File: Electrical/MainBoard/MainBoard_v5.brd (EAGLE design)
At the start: 100 x 100 mm, 117 parts, among them IC1 MEGA1284-P, IC2 MCP4922-E/SL, IC3 MCP4921-E/SN, IC4 TL074D, IC5 TL074D, IC6 FT232RL, Q1 BC140-10, Q2 BC160, Q3 BC140-10, Q4 BC160, Q5 BD239, Q6 BC547, Q7 BC557, Q8 16MHz, X1 FH12-45S-0.5SH, X2 22-23-2021, X3 PN61729-S

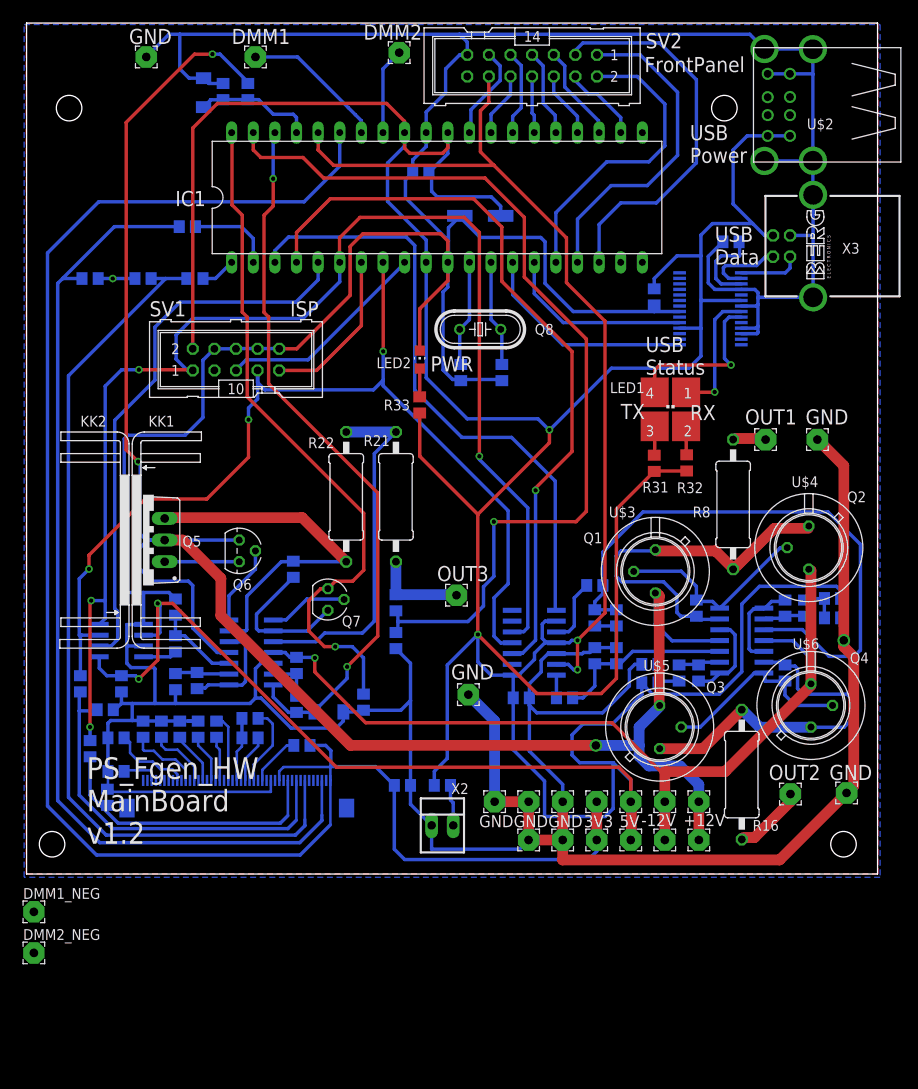
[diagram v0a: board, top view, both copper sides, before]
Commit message: Updated OutputControls and MainBoard in Electrical folder
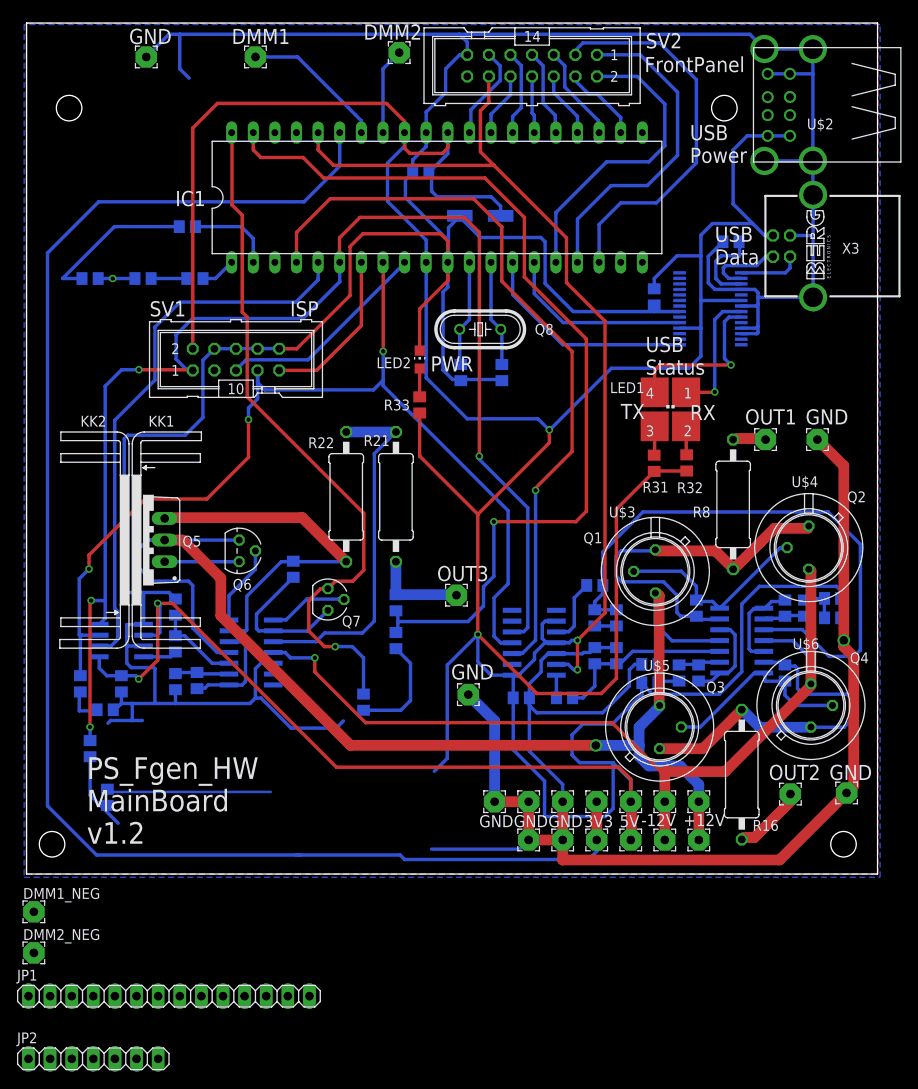
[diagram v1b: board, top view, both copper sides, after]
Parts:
- removed C12, C13, C14, C15, C16, C17, C18, C19, C20, C21, C22: 4u7, rcl:C0805
- removed D3, D4: 5V, diode:SOD80C
- removed R27: 240k, OwnDevices:R0805
- removed R28, R30: 100k, OwnDevices:R0805
- removed R29: 150k, OwnDevices:R0805
- removed R34: 10R, rcl:R0805
- removed X1: FH12-45S-0.5SH, con-hirose:FH12-45S-0.5SH
- removed X2: 22-23-2021, con-molex:22-23-2021
- added JP1: PINHD-1X14, Connector:1X14
- added JP2: PINHD-1X7, Connector:1X07
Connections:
- net LCD_A0 renamed LCD_DC
- removed net !DDS_LDAC: IC1.3, IC2.8
- removed net +12V_VOLT: D4.C, IC1.37, R29.1, R30.2
- removed net -12V_VOLT: D3.C, IC1.38, IC5.14, R28.1
- removed net BL_A: R34.2, X2.2
- removed net CAP1+: C15.1, X1.21
- removed net CAP1-: C14.2, C15.2, X1.23
- removed net CAP2+: C16.1, X1.27
- removed net CAP2-: C16.2, X1.25
- removed net CAP3+: C14.1, X1.19
- removed net LCD_A0_3V3: R40.1, R44.1, X1.7
- removed net MV1: C21.1, X1.37
- removed net MV2: C22.1, X1.43
- removed net N$27: IC5.13, R27.1, R28.2
- removed net V1: C17.1, X1.29
- removed net V2: C18.1, X1.31
- removed net V3: C19.1, X1.33
- removed net VC: C20.1, X1.35
- removed net VOUT: C13.1, X1.17
- new net !IO_EXP_CS: IC1.3, JP2.5
- new net !TS_CS: IC1.37, JP1.11
- new net IO_EXP_INT: IC1.21, JP2.6
- new net N$21: JP1.5, R40.1, R44.1
- new net TS_IRQ: IC1.38, JP1.14
- net !LCD_CS_3V3: now also JP1.3; no longer X1.3
- net +12V: no longer R29.2
- net +3V3: now also JP1.4, JP1.8; no longer C12.1, C13.2, X1.1, X1.13
- net +5V: now also JP1.1, JP2.1; no longer R34.1
- net -12V: no longer R27.2
- net GND: now also IC2.8, JP1.2, JP2.7; no longer C12.2, C17.2, C18.2, C19.2, C20.2, C21.2, C22.2, D3.A, D4.A, IC5.12, R30.1, X1.15, X2.1
- net MISO: now also JP1.13, JP2.4
- net MOSI: now also JP1.12, JP2.3
- net MOSI_3V3: now also JP1.6; no longer X1.11
- net SCK: now also JP1.10, JP2.2
- net SCK_3V3: now also JP1.7; no longer X1.9
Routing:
- net LCD_A0_3V3: track 105.3 -> 0.00 mm
- net !LCD_CS_3V3: track 119.0 -> 18.5 mm
- net -12V_VOLT: track 84.2 -> 0.00 mm, vias 2 -> 0
- net !DDS_LDAC: track 72.1 -> 0.00 mm
- net +12V: track 219.2 -> 149.7 mm, vias 3 -> 1
- net GND: track 666.7 -> 622.7 mm
- net SCK_3V3: track 46.6 -> 4.43 mm
- net +3V3: track 209.7 -> 181.3 mm
- net MOSI_3V3: track 34.2 -> 9.79 mm
- net +12V_VOLT: track 14.0 -> 0.00 mm
- net CAP3+: track 9.56 -> 0.00 mm
- net MV1: track 9.49 -> 0.00 mm
- net VC: track 8.71 -> 0.00 mm
- net CAP2-: track 7.95 -> 0.00 mm
- net CAP1-: track 7.54 -> 0.00 mm
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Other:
- board text removed: "GLCD"
